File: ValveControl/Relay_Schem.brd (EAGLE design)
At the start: 101.6 x 53.6 mm, 69 parts, among them M1 IRLZ44, M2 IRLZ44, M3 IRLZ44, M4 IRLZ44, Q1 LINEAR_REGULATOR, Q2 LINEAR_REGULATOR, Q3 LINEAR_REGULATOR, Q4 LINEAR_REGULATOR, Q5 LINEAR_REGULATOR

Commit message: More final tweaks to valve board layout
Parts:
- moved D4 0.25 mm to (16.0, 31.2)
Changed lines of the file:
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@@
 <attribute name="POPULARITY" value="0" x="16.002" y="36.068" size="1.778" layer="27" display="off"/>
 </element>
-<element name="D4" library="diode" library_urn="urn:adsk.eagle:library:210" package="DO15-12" package3d_urn="urn:adsk.eagle:package:43369/2" value="1N5060GP" x="15.748" y="31.242" smashed="yes">
-<attribute name="NAME" x="12.065" y="33.401" size="1.27" layer="25" ratio="10"/>
-<attribute name="POPULARITY" value="0" x="15.748" y="31.242" size="1.778" layer="27" display="off"/>
+<element name="D4" library="diode" library_urn="urn:adsk.eagle:library:210" package="DO15-12" package3d_urn="urn:adsk.eagle:package:43369/2" value="1N5060GP" x="16.002" y="31.242" smashed="yes">
+<attribute name="NAME" x="12.319" y="33.401" size="1.27" layer="25" ratio="10"/>
+<attribute name="POPULARITY" value="0" x="16.002" y="31.242" size="1.778" layer="27" display="off"/>
 </element>
 <element name="MSEL" library="led" library_urn="urn:adsk.eagle:library:259" package="LED3MM" package3d_urn="urn:adsk.eagle:package:15797/1" value="" x="29.845" y="6.985" smashed="yes">
@@
 <element name="M1" library="LPRD_RELAY" package="TO220V" value="IRLZ44" x="25.654" y="43.688" smashed="yes" rot="R90">
 <attribute name="NAME" x="31.6992" y="38.608" size="1.27" layer="25" ratio="10" rot="R90"/>
-<attribute name="VALUE" x="33.274" y="38.608" size="1.27" layer="27" ratio="10" rot="R90"/>
 <attribute name="_EXTERNAL_" value="" x="25.654" y="43.688" size="1.778" layer="27" rot="R90" display="off"/>
 </element>
 <element name="M2" library="LPRD_RELAY" package="TO220V" value="IRLZ44" x="25.654" y="32.766" smashed="yes" rot="R90">
 <attribute name="NAME" x="31.6992" y="27.686" size="1.27" layer="25" ratio="10" rot="R90"/>
-<attribute name="VALUE" x="33.274" y="27.686" size="1.27" layer="27" ratio="10" rot="R90"/>
 <attribute name="_EXTERNAL_" value="" x="25.654" y="32.766" size="1.778" layer="27" rot="R90" display="off"/>
 </element>
 <element name="M3" library="LPRD_RELAY" package="TO220V" value="IRLZ44" x="35.306" y="43.688" smashed="yes" rot="R90">
 <attribute name="NAME" x="41.3512" y="38.608" size="1.27" layer="25" ratio="10" rot="R90"/>
-<attribute name="VALUE" x="42.926" y="38.608" size="1.27" layer="27" ratio="10" rot="R90"/>
 <attribute name="_EXTERNAL_" value="" x="35.306" y="43.688" size="1.778" layer="27" rot="R90" display="off"/>
 </element>
 <element name="M4" library="LPRD_RELAY" package="TO220V" value="IRLZ44" x="35.306" y="32.766" smashed="yes" rot="R90">
 <attribute name="NAME" x="41.3512" y="27.686" size="1.27" layer="25" ratio="10" rot="R90"/>
-<attribute name="VALUE" x="42.926" y="27.686" size="1.27" layer="27" ratio="10" rot="R90"/>
 <attribute name="_EXTERNAL_" value="" x="35.306" y="32.766" size="1.778" layer="27" rot="R90" display="off"/>
 </element>
@@
 <contactref element="VAL_OUT" pad="P$4"/>
 <contactref element="M4" pad="2"/>
-<wire x1="2.8575" y1="37.7825" x2="2.8575" y2="38.4175" width="0.508" layer="1"/>
+<wire x1="2.8575" y1="38.0365" x2="2.8575" y2="38.4175" width="0.508" layer="1"/>
 <wire x1="2.8575" y1="38.4175" x2="2.794" y2="38.608" width="0.254" layer="1"/>
-<wire x1="2.8575" y1="37.7825" x2="9.398" y2="31.242" width="0.508" layer="1"/>
+<wire x1="2.8575" y1="38.0365" x2="9.652" y2="31.242" width="0.508" layer="1"/>
 <wire x1="37.1475" y1="32.0675" x2="37.846" y2="32.766" width="0.508" layer="16"/>
 <wire x1="30.607" y1="32.0675" x2="37.1475" y2="32.0675" width="0.508" layer="16"/>
@@
 <wire x1="23.749" y1="32.893" x2="25.2095" y2="31.4325" width="0.508" layer="16"/>
 <wire x1="10.9855" y1="32.893" x2="23.749" y2="32.893" width="0.508" layer="16"/>
-<wire x1="9.525" y1="31.4325" x2="10.9855" y2="32.893" width="0.508" layer="16"/>
-<wire x1="9.525" y1="31.4325" x2="9.398" y2="31.242" width="0.254" layer="16"/>
+<wire x1="10.287" y1="32.1945" x2="10.9855" y2="32.893" width="0.508" layer="16"/>
+<wire x1="10.287" y1="32.1945" x2="9.652" y2="31.242" width="0.254" layer="16"/>
 </signal>
 <signal name="N$10">

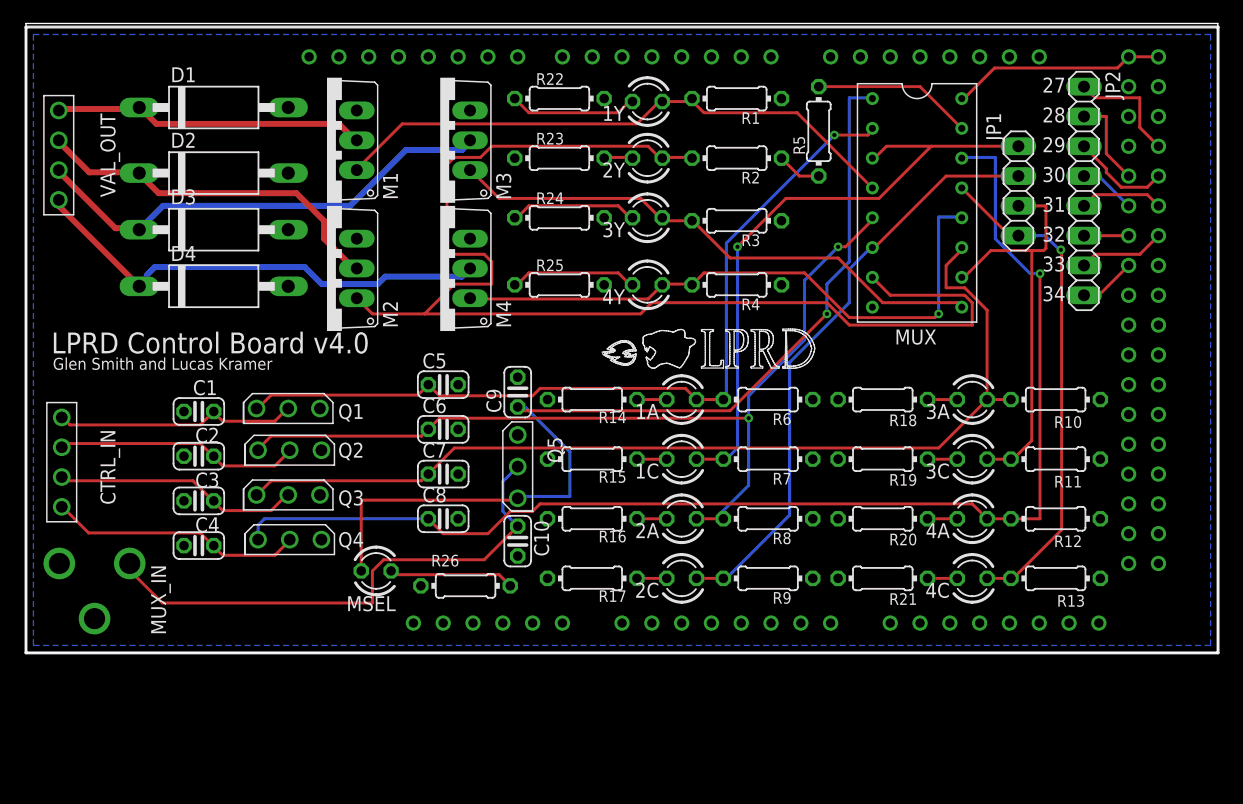
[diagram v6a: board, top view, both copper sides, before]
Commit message: Remove diodes, fix some slight layout issues
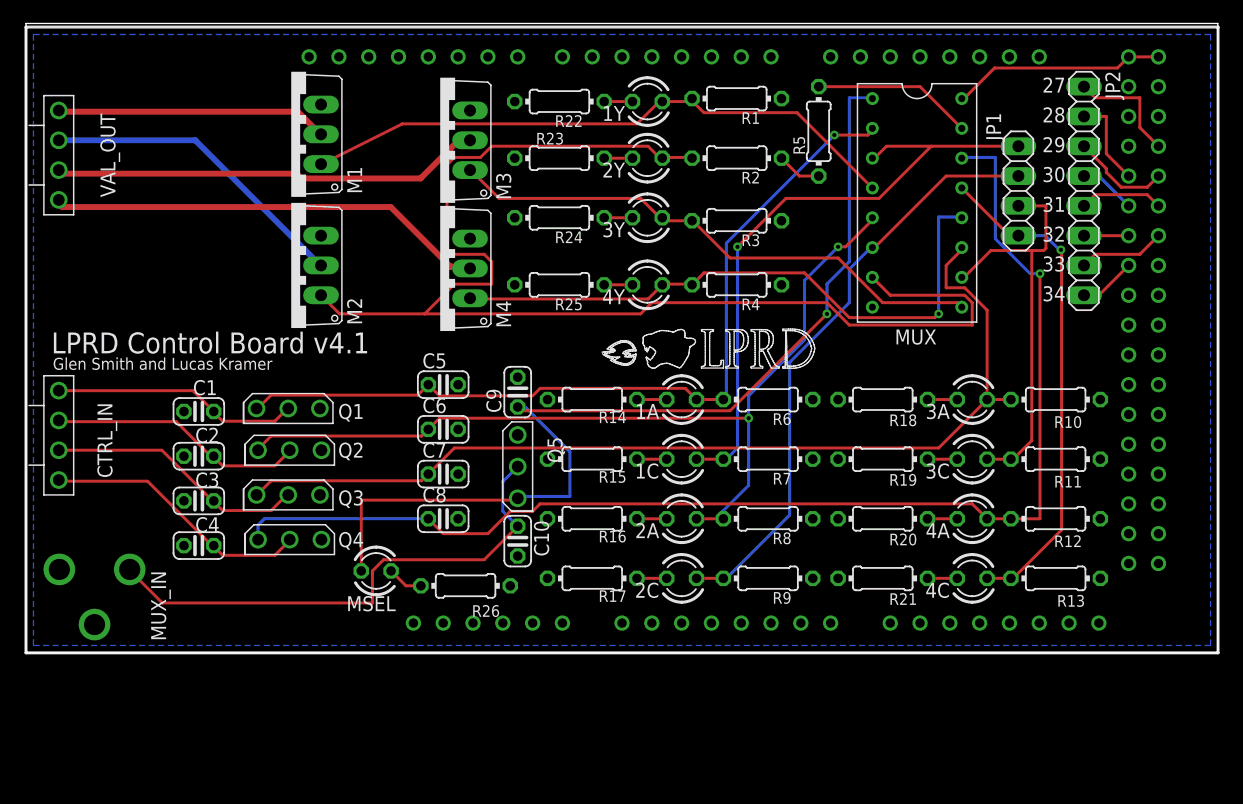
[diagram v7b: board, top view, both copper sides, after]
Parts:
- removed D1, D2, D3, D4: 1N5060GP, diode:DO15-12
- moved M1 3.09 mm to (22.6, 44.2)
- moved M2 3.06 mm to (22.6, 33.0)
- moved CTRL_IN 2.30 mm to (2.79, 17.3)
- moved MUX_IN 0.51 mm to (5.84, 7.11)
- moved R22 0.25 mm to (45.5, 47.0), turned to 180 degrees
- turned R24 to 180 degrees
- turned R25 to 180 degrees
- turned R26 to 0 degrees
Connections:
- net 0: no longer D1.A, D2.A, D3.A, D4.A
- net N$3: no longer D1.C
- net N$5: no longer D2.C
- net N$8: no longer D3.C
- net N$9: no longer D4.C
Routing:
- net N$11: track 10.9 -> 2.41 mm
- net N$23: track 10.8 -> 2.41 mm
- net N$22: track 10.8 -> 2.41 mm
- net N$7: track 10.7 -> 3.07 mm
- net N$5: track 30.9 -> 26.8 mm
- net N$8: track 40.4 -> 37.0 mm
- net N$3: track 26.7 -> 23.3 mm
- net 2Y: track 107.8 -> 111.0 mm
- net N$9: track 40.3 -> 37.9 mm
- net 1Y: track 49.7 -> 51.9 mm
- net N$4: track 21.0 -> 22.5 mm
- net N$12: track 21.7 -> 23.2 mm
- net N$2: track 21.0 -> 22.0 mm
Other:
- board text added: "LPRD Control Board v4.1"
- board text removed: "LPRD Control Board v4.0"
